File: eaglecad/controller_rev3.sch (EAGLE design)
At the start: 91 parts, among them J1 1.27MM-SWD-CONNECTOR, U100 STM32F042K6, U101 TCAN330, U200 TPS63070, U300 STSPIN230, U301 TSV991ILT, U302 AS5047P, U400 STSPIN250, U401 TSV991ILT, X101 16MHZ-2.5x2mm

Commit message: rev 3 progress
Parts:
- removed JP101: (no value), pinhead:PINHD-1X4
- added JP103: (no value), SparkFun-Connectors:6_PIN_SERIAL_TARGETSILK
- added JP301: (no value), pinhead-2:PINHD-1X03_2.00
- JP1: device pinhead:PINHD-1X3 -> pinhead:PINHD-1X2
- JP102: device SparkFun-Connectors:6_PIN_SERIAL_TARGETSILK -> pinhead:PINHD-1X2
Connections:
- net CAN_H: now also JP102.1; no longer JP101.2
- net CAN_L: now also JP102.2; no longer JP101.3
- net GND: now also JP1.2, JP103.GND; no longer JP101.4, JP102.GND
- net PA2/USART2_TX: now also JP103.TXO; no longer JP102.TXO
- net PA3/USART2_RX: now also JP103.RXI; no longer JP102.RXI
- net TPS-FB: no longer PG.TP
- net TPS-PG: now also PG.TP
- net U: now also JP301.1; no longer JP1.1
- net V: now also JP301.2; no longer JP1.2
- net V_BATT: now also JP1.1, JP103.VCC; no longer JP101.1
- net W: now also JP301.3; no longer JP1.3
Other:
- moved on the sheet: C105, PG

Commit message: some more cleanup on rev 3
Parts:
- removed H1, H2, H3, H4: STAND-OFFTIGHT, SparkFun-Hardware:STAND-OFFTIGHT
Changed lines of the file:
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@@
 <part name="JP103" library="SparkFun-Connectors" library_urn="urn:adsk.eagle:library:513" deviceset="6_PIN_SERIAL_TARGET" device="SILK" package3d_urn="urn:adsk.eagle:package:37995/1"/>
 <part name="GND6" library="supply1" deviceset="GND" device=""/>
-<part name="H1" library="SparkFun-Hardware" library_urn="urn:adsk.eagle:library:519" deviceset="STAND-OFF" device="TIGHT" package3d_urn="urn:adsk.eagle:package:38629/1"/>
-<part name="H2" library="SparkFun-Hardware" library_urn="urn:adsk.eagle:library:519" deviceset="STAND-OFF" device="TIGHT" package3d_urn="urn:adsk.eagle:package:38629/1"/>
-<part name="H3" library="SparkFun-Hardware" library_urn="urn:adsk.eagle:library:519" deviceset="STAND-OFF" device="TIGHT" package3d_urn="urn:adsk.eagle:package:38629/1"/>
-<part name="H4" library="SparkFun-Hardware" library_urn="urn:adsk.eagle:library:519" deviceset="STAND-OFF" device="TIGHT" package3d_urn="urn:adsk.eagle:package:38629/1"/>
 <part name="FRAME2" library="frames" library_urn="urn:adsk.eagle:library:229" deviceset="FRAME_B_L" device=""/>
 <part name="SUPPLY12" library="SparkFun-PowerSymbols" library_urn="urn:adsk.eagle:library:530" deviceset="V_BATT" device=""/>
@@
 <instance part="JP103" gate="G$1" x="149.86" y="63.5"/>
 <instance part="GND6" gate="1" x="166.37" y="68.58" rot="MR0"/>
-<instance part="H1" gate="G$1" x="297.18" y="16.51"/>
-<instance part="H2" gate="G$1" x="299.72" y="16.51"/>
-<instance part="H3" gate="G$1" x="302.26" y="16.51"/>
-<instance part="H4" gate="G$1" x="304.8" y="16.51"/>
 <instance part="SUPPLY2" gate="G$1" x="91.44" y="127"/>
 <instance part="GND3" gate="1" x="91.44" y="119.38" rot="MR0"/>

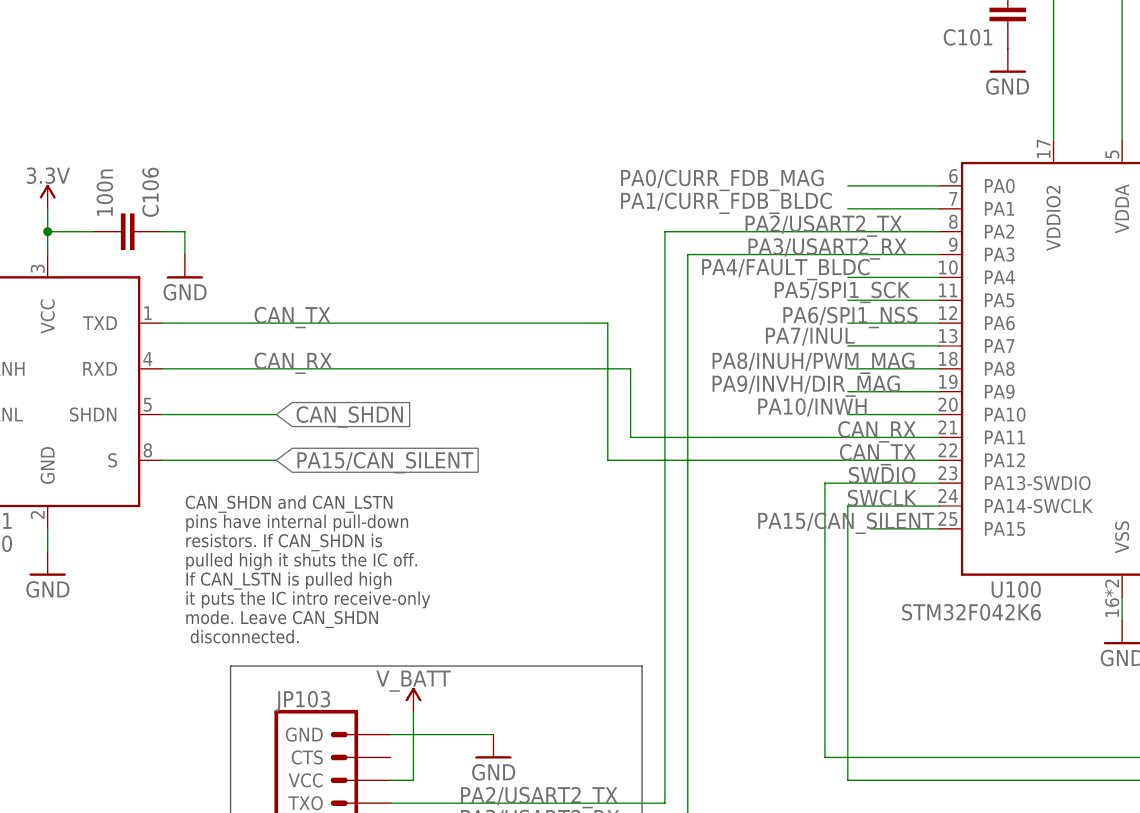
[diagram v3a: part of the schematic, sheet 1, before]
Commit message: Clean up from last week: added three test points because test points are important when you might need a signal, and added signal names because N names are dumb, and cleaned up a few ERC warnings. And, Eric, added the damn board name! Sheesh, whose board is this, anyway?? ;)
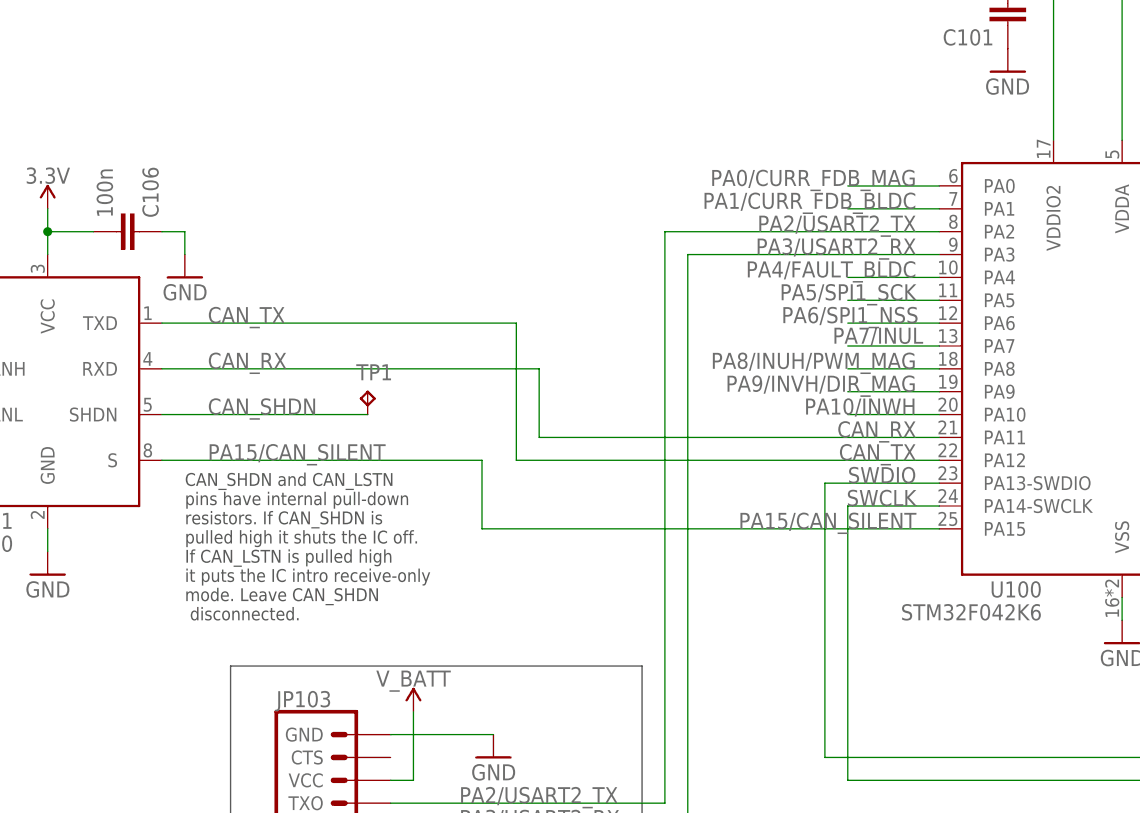
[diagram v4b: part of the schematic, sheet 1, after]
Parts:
- added TP1, TP2, TP3: TPTP06R, testpad:TPTP06R
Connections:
- net N$1 renamed AS5047_MOSI
- net N$13 renamed QUAD_B
- net N$14 renamed BLDC-I-IN-
- net N$15 renamed MAG-I-IN+
- net N$16 renamed BLDC-I-IN+
- net N$17 renamed MAG-I-IN-
- net N$19 renamed 250_TOFF
- net N$25 renamed 250_REF
- net N$27 renamed MAG-I-OUT
- net N$29 renamed BLDC-I-OUT
- net N$4 renamed QUAD_A
- net CAN_SHDN: now also TP1.TP
- net STBY/RESET_BLDC: now also TP2.TP
- net STBY/RESET_MAG: now also TP3.TP

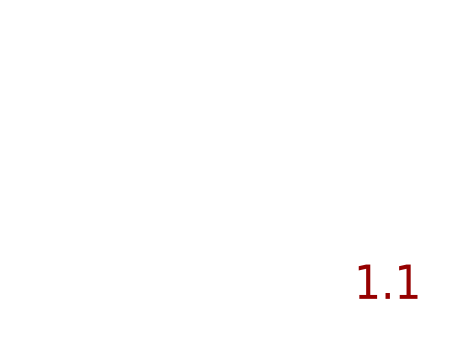
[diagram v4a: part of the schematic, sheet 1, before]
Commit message: The frame said Rev 1.1. I fixed that to say Rev 3.
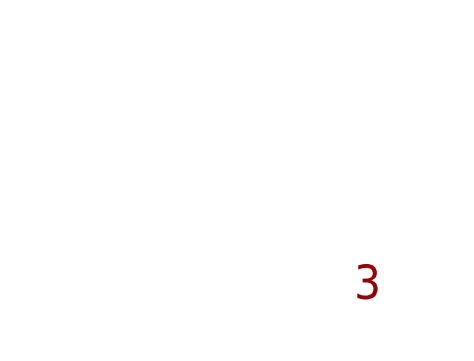
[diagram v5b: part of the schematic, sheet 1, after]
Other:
- note added: "3"
- note removed: "1.1"
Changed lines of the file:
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@@
 <?xml version="1.0" encoding="utf-8"?>
 <!DOCTYPE eagle SYSTEM "eagle.dtd">
-<eagle version="9.0.1">
+<eagle version="8.6.0">
 <drawing>
 <settings>
@@
 built in</text>
 <text x="341.63" y="26.67" size="3.81" layer="94">ACS Controller</text>
-<text x="416.56" y="6.35" size="3.81" layer="94">1.1</text>
+<text x="416.56" y="6.35" size="3.81" layer="94">3</text>
 <text x="11.43" y="5.08" size="1.778" layer="97">All resistors 0402 +/- 1% unless marked</text>
 <text x="11.43" y="2.54" size="1.778" layer="97">All caps are ceramic 10% X5R &gt;= 16V Vwv unless marked</text>
